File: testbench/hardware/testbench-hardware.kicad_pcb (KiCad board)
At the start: 2 copper layers, 88.9 x 88.9 mm, 43 parts, among them J1 ZIF DIP-16 Socket, Q1 ZTX458, SW1 Action, SW2 Mode Select, SW3 Enable Power

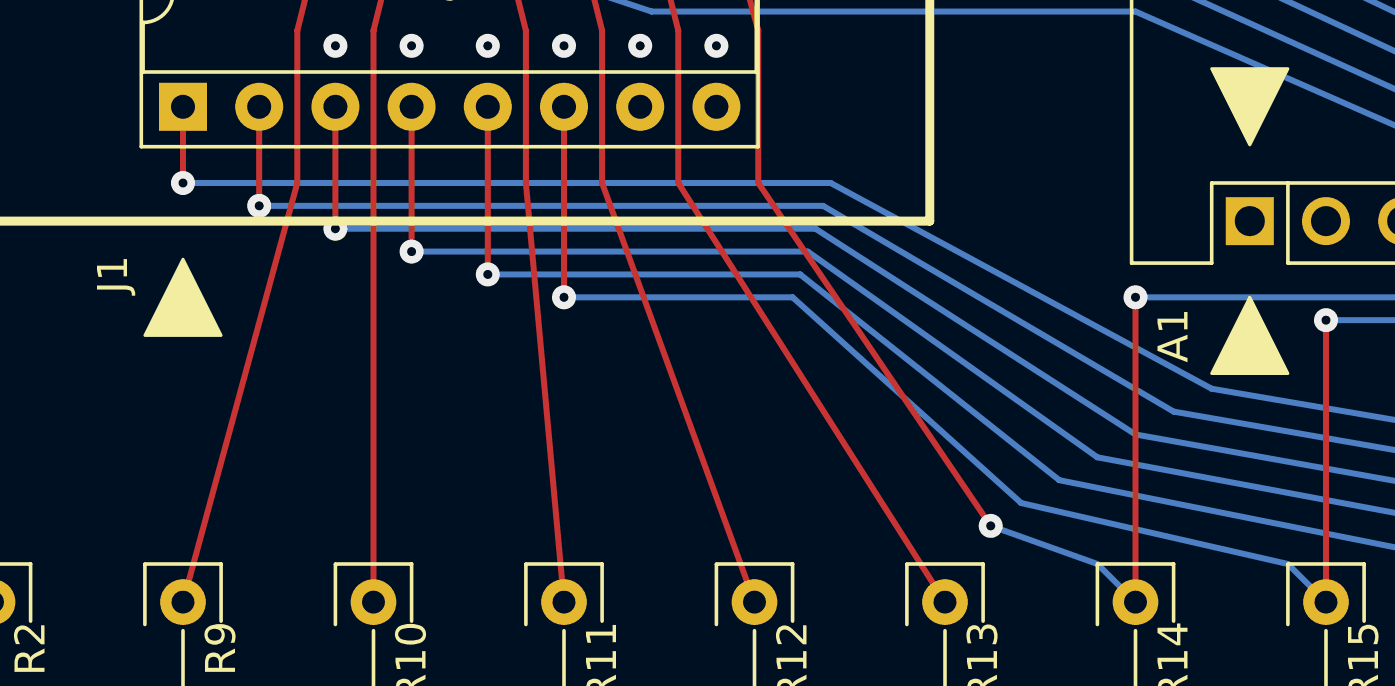
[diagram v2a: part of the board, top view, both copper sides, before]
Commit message: [testbench][hardware] Tweaked the layout of some traces
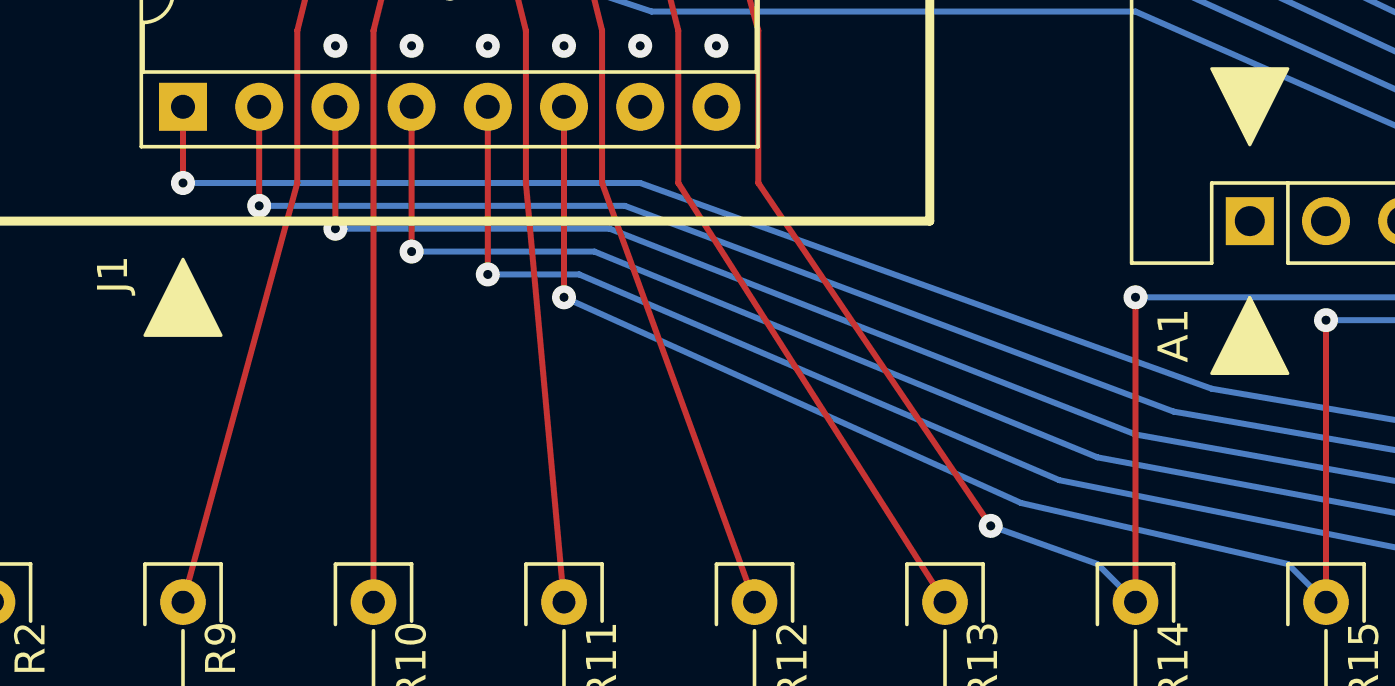
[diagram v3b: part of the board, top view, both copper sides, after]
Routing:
- net /B1: track 68.2 -> 67.1 mm
- net /B0: track 71.7 -> 70.7 mm
- net /V1: track 75.3 -> 74.5 mm
- net /V0: track 79.0 -> 78.3 mm
- net /R1: track 83.4 -> 82.7 mm
- net /R0: track 110.5 -> 109.9 mm
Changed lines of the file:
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@@
   (via (at 146.05 102.87) (size 0.8) (drill 0.3) (layers "F.Cu" "B.Cu") (net 11))
   (segment (start 137.16 100.33) (end 139.7 102.87) (width 0.2) (layer "B.Cu") (net 11))
-  (segment (start 76.2 114.3) (end 97.79 114.3) (width 0.2) (layer "B.Cu") (net 11))
   (segment (start 139.7 102.87) (end 140.8 102.87) (width 0.2) (layer "B.Cu") (net 11))
   (segment (start 144.78 127) (end 146.05 128.27) (width 0.2) (layer "B.Cu") (net 11))
-  (segment (start 110.49 121.158) (end 97.79 114.3) (width 0.2) (layer "B.Cu") (net 11))
+  (segment (start 76.2 114.3) (end 91.44 114.3) (width 0.2) (layer "B.Cu") (net 11))
   (segment (start 146.05 102.87) (end 140.8 102.87) (width 0.2) (layer "B.Cu") (net 11))
+  (segment (start 91.44 114.3) (end 110.49 121.158) (width 0.2) (layer "B.Cu") (net 11))
   (segment (start 144.78 127) (end 110.49 121.158) (width 0.2) (layer "B.Cu") (net 11))
   (segment (start 139.7 128.27) (end 139.7 121.92) (width 0.2) (layer "F.Cu") (net 12))
@@
   (via (at 139.7 121.92) (size 0.8) (drill 0.3) (layers "F.Cu" "B.Cu") (net 12))
   (segment (start 145.923 116.967) (end 147.32 115.57) (width 0.2) (layer "B.Cu") (net 12))
+  (segment (start 90.932 115.062) (end 78.74 115.062) (width 0.2) (layer "B.Cu") (net 12))
   (segment (start 139.7 121.92) (end 145.923 116.967) (width 0.2) (layer "B.Cu") (net 12))
+  (segment (start 90.932 115.062) (end 109.22 121.92) (width 0.2) (layer "B.Cu") (net 12))
   (segment (start 139.7 128.27) (end 138.43 127) (width 0.2) (layer "B.Cu") (net 12))
-  (segment (start 109.22 121.92) (end 97.536 115.062) (width 0.2) (layer "B.Cu") (net 12))
-  (segment (start 97.536 115.062) (end 78.74 115.062) (width 0.2) (layer "B.Cu") (net 12))
   (segment (start 138.43 127) (end 109.22 121.92) (width 0.2) (layer "B.Cu") (net 12))
   (segment (start 133.35 128.27) (end 133.35 121.158) (width 0.2) (layer "F.Cu") (net 13))
@@
   (via (at 133.35 121.158) (size 0.8) (drill 0.3) (layers "F.Cu" "B.Cu") (net 13))
   (via (at 81.28 115.824) (size 0.8) (drill 0.3) (layers "F.Cu" "B.Cu") (net 13))
-  (segment (start 107.95 122.682) (end 97.282 115.824) (width 0.2) (layer "B.Cu") (net 13))
+  (segment (start 81.28 115.824) (end 90.424 115.824) (width 0.2) (layer "B.Cu") (net 13))
   (segment (start 132.08 127) (end 107.95 122.682) (width 0.2) (layer "B.Cu") (net 13))
-  (segment (start 81.28 115.824) (end 97.282 115.824) (width 0.2) (layer "B.Cu") (net 13))
+  (segment (start 90.424 115.824) (end 107.95 122.682) (width 0.2) (layer "B.Cu") (net 13))
   (segment (start 132.08 127) (end 133.35 128.27) (width 0.2) (layer "B.Cu") (net 13))
   (segment (start 143.383 116.967) (end 144.78 115.57) (width 0.2) (layer "B.Cu") (net 13))
@@
   (via (at 127 120.396) (size 0.8) (drill 0.3) (layers "F.Cu" "B.Cu") (net 14))
   (via (at 83.82 116.586) (size 0.8) (drill 0.3) (layers "F.Cu" "B.Cu") (net 14))
-  (segment (start 106.68 123.444) (end 97.028 116.586) (width 0.2) (layer "B.Cu") (net 14))
+  (segment (start 89.916 116.586) (end 106.68 123.444) (width 0.2) (layer "B.Cu") (net 14))
   (segment (start 125.73 127) (end 127 128.27) (width 0.2) (layer "B.Cu") (net 14))
   (segment (start 127 120.396) (end 130.81 120.396) (width 0.2) (layer "B.Cu") (net 14))
-  (segment (start 83.82 116.586) (end 97.028 116.586) (width 0.2) (layer "B.Cu") (net 14))
   (segment (start 125.73 127) (end 106.68 123.444) (width 0.2) (layer "B.Cu") (net 14))
   (segment (start 130.81 120.396) (end 140.843 116.967) (width 0.2) (layer "B.Cu") (net 14))
   (segment (start 140.843 116.967) (end 142.24 115.57) (width 0.2) (layer "B.Cu") (net 14))
+  (segment (start 83.82 116.586) (end 89.916 116.586) (width 0.2) (layer "B.Cu") (net 14))
   (segment (start 120.65 128.27) (end 120.65 119.634) (width 0.2) (layer "F.Cu") (net 15))
   (segment (start 86.36 111.76) (end 86.36 117.348) (width 0.2) (layer "F.Cu") (net 15))
@@
   (segment (start 138.303 116.967) (end 139.7 115.57) (width 0.2) (layer "B.Cu") (net 15))
   (segment (start 119.38 127) (end 105.41 124.206) (width 0.2) (layer "B.Cu") (net 15))
-  (segment (start 105.41 124.206) (end 96.774 117.348) (width 0.2) (layer "B.Cu") (net 15))
-  (segment (start 86.36 117.348) (end 96.774 117.348) (width 0.2) (layer "B.Cu") (net 15))
+  (segment (start 86.36 117.348) (end 89.408 117.348) (width 0.2) (layer "B.Cu") (net 15))
+  (segment (start 89.408 117.348) (end 105.41 124.206) (width 0.2) (layer "B.Cu") (net 15))
   (segment (start 138.6205 99.2505) (end 139.7 100.33) (width 0.2) (layer "B.Cu") (net 19))
   (segment (start 133.35 98.263676) (end 138.6205 99.2505) (width 0.2) (layer "B.Cu") (net 19))
@@
   (via (at 114.3 118.872) (size 0.8) (drill 0.3) (layers "F.Cu" "B.Cu") (net 26))
   (via (at 88.9 118.11) (size 0.8) (drill 0.3) (layers "F.Cu" "B.Cu") (net 26))
-  (segment (start 88.9 118.11) (end 96.52 118.11) (width 0.2) (layer "B.Cu") (net 26))
   (segment (start 128.27 118.872) (end 135.763 116.967) (width 0.2) (layer "B.Cu") (net 26))
   (segment (start 113.03 127) (end 104.14 124.968) (width 0.2) (layer "B.Cu") (net 26))
+  (segment (start 88.9 118.11) (end 104.14 124.968) (width 0.2) (layer "B.Cu") (net 26))
   (segment (start 135.763 116.967) (end 137.16 115.57) (width 0.2) (layer "B.Cu") (net 26))
   (segment (start 114.3 118.872) (end 128.27 118.872) (width 0.2) (layer "B.Cu") (net 26))
   (segment (start 113.03 127) (end 114.3 128.27) (width 0.2) (layer "B.Cu") (net 26))
-  (segment (start 104.14 124.968) (end 96.52 118.11) (width 0.2) (layer "B.Cu") (net 26))
   (segment (start 111.19 77.5) (end 111.19 82.55) (width 1.27) (layer "F.Cu") (net 27))
   (segment (start 134.62 77.53) (end 134.62 74.93) (width 1.27) (layer "F.Cu") (net 27))

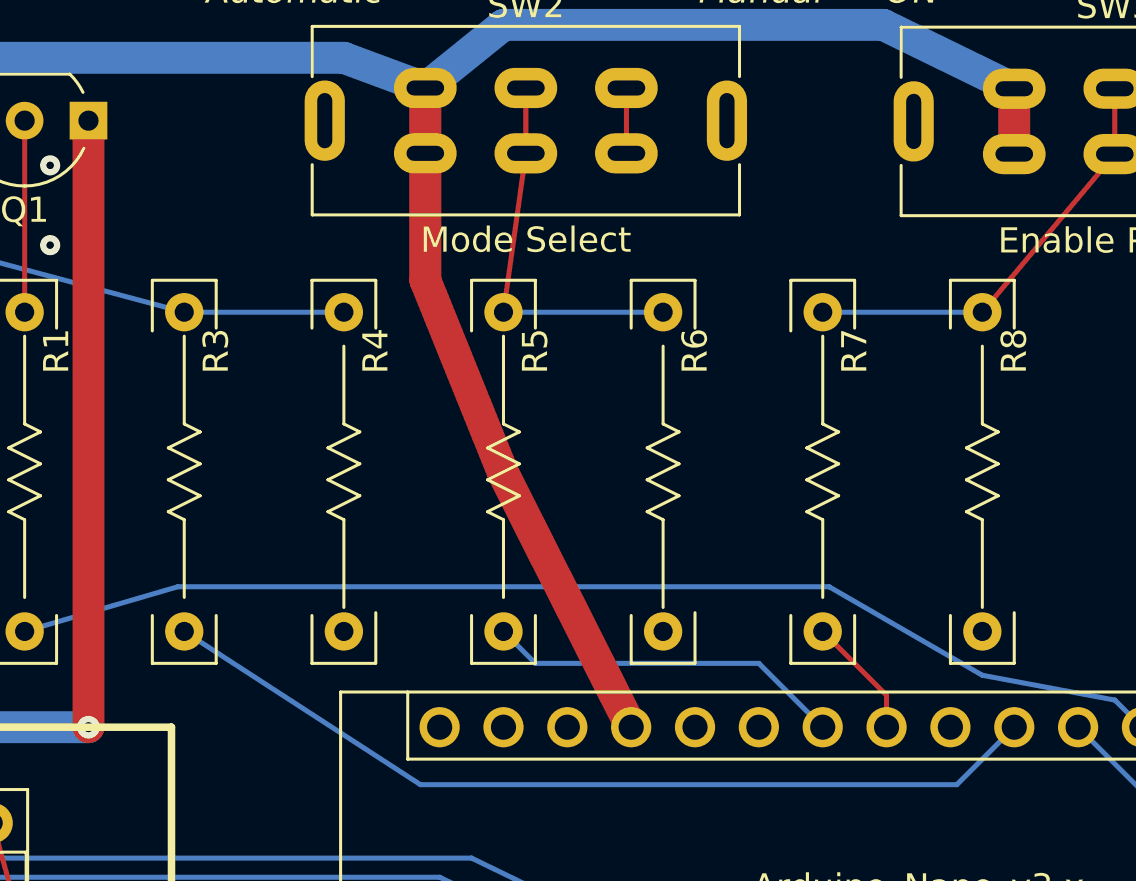
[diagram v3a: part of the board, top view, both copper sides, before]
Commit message: Fixes #3 : [bug][testbench] remove R3, R5 and R7
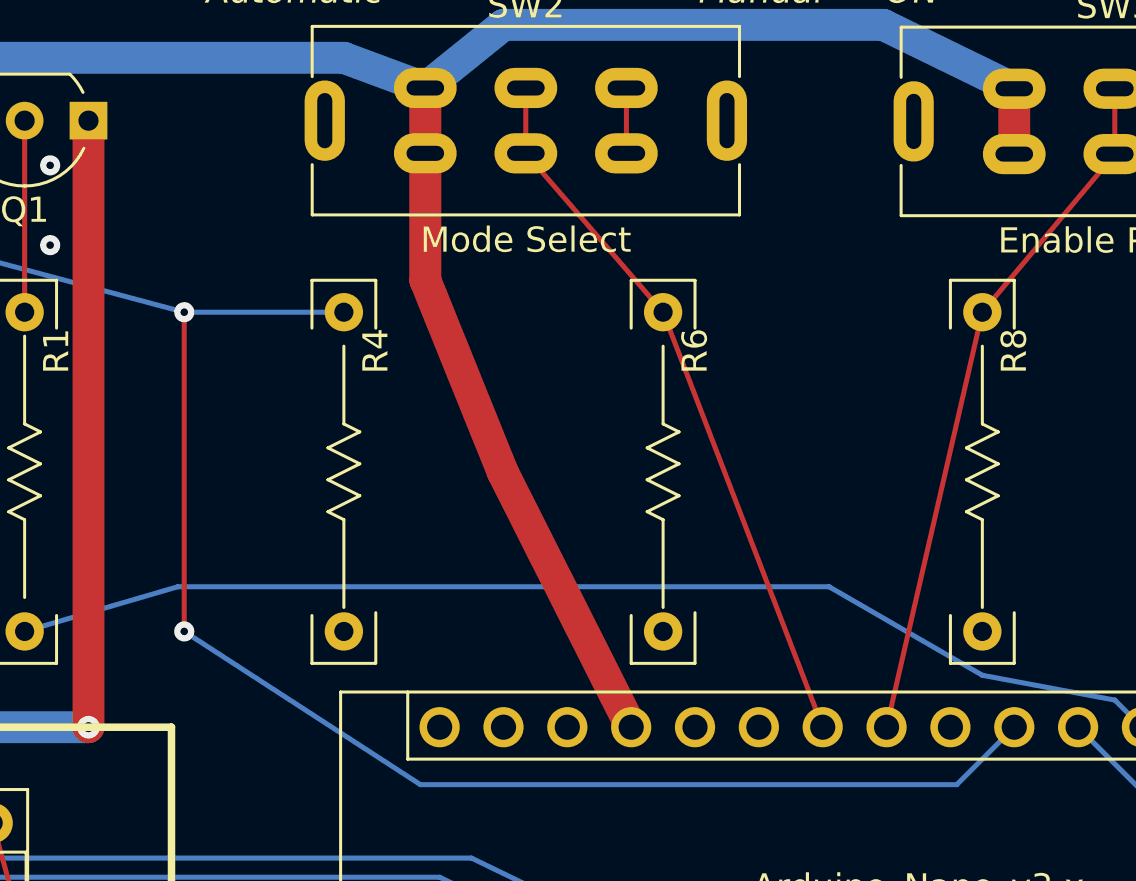
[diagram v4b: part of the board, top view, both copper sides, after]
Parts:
- removed R3, R5, R7: 10K, commons-passives_THT:Passive_THT_resistor_W2.54mm_L12.70mm
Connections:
- R4 pad 2: Net-(R3-Pad1) -> /ACTION_BUTTON
- R6 pad 2: Net-(SW2-B) -> /MODE_SWITCH
- R8 pad 2: Net-(SW3-B) -> /POWER_ENABLE_SWITCH
- SW1 pad 2: Net-(R3-Pad1) -> /ACTION_BUTTON
- SW2 pad 2: Net-(SW2-B) -> /MODE_SWITCH
- SW3 pad 2: Net-(SW3-B) -> /POWER_ENABLE_SWITCH
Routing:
- net /ACTION_BUTTON: track 35.8 -> 87.1 mm, vias 0 -> 2
- net Net-(R3-Pad1): track 38.7 -> 0.00 mm
- net /POWER_ENABLE_SWITCH: track 4.86 -> 27.7 mm
- net Net-(SW3-B): track 17.2 -> 0.00 mm
- net Net-(SW2-B): track 15.3 -> 0.00 mm
- net /MODE_SWITCH: track 14.3 -> 28.6 mm
